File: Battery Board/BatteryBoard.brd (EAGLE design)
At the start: 25.4 x 50.8 mm, 28 parts, among them IC1 TPS63060DSCT, J0 1725656, Q1 IAUC60N04S6L030HATMA1, U0 STM32L031K4U6, U1 MCP73831T-2ATI_OT, U3 STM809TWX6F

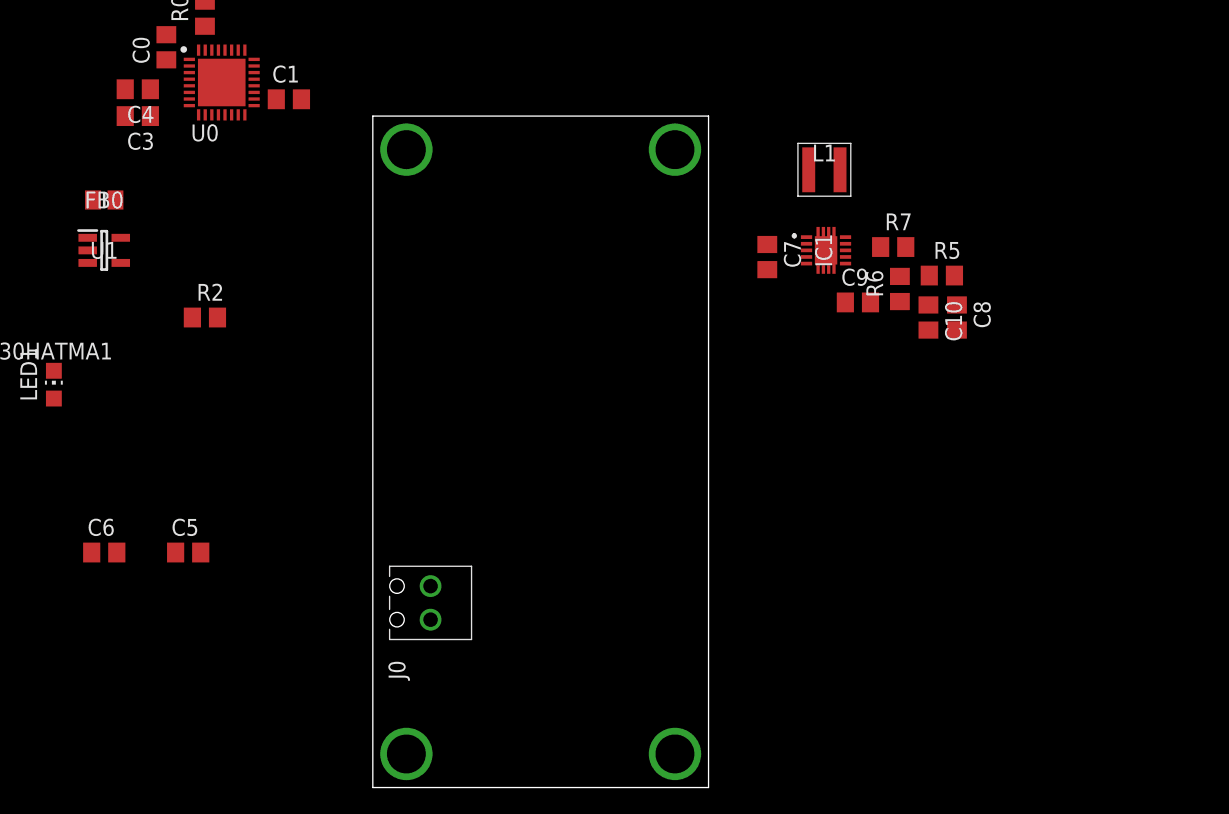
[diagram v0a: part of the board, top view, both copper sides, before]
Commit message: added switch jumper
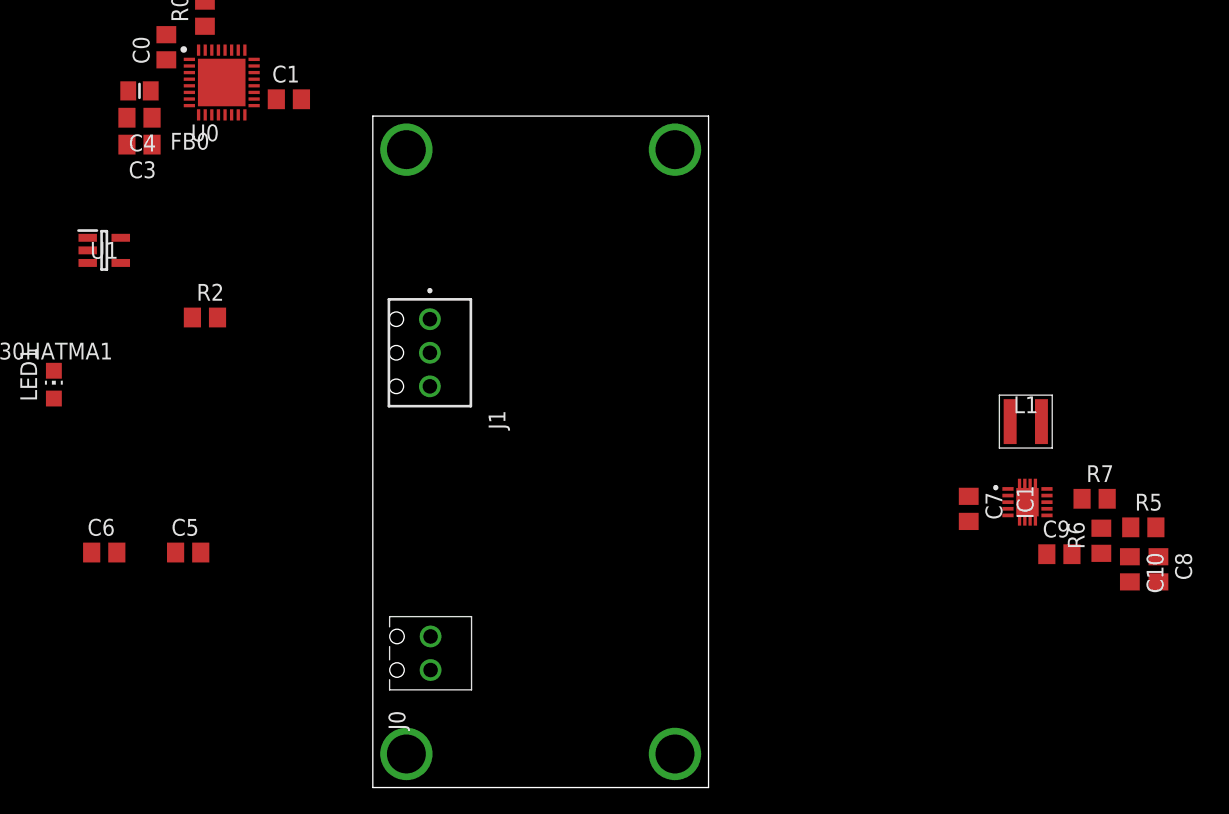
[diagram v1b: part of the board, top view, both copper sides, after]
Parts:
- added J1: 1725669, SamacSys_Parts:1725669
- moved C10 24.4 mm to (44.6, -8.89)
- moved C8 24.4 mm to (46.7, -8.89)
- moved C9 24.4 mm to (39.2, -7.75)
- moved IC1 24.4 mm to (36.8, -3.81)
- moved L1 24.4 mm to (36.7, 2.29)
- moved R5 24.4 mm to (45.6, -5.71)
- moved R6 24.4 mm to (42.4, -6.73)
- moved C7 24.4 mm to (32.4, -4.32)
- moved R7 24.4 mm to (41.9, -3.56)
- moved FB0 8.68 mm to (-30.4, 27.3)
- moved J0 3.81 mm to (-11.4, -15.2)
- moved C3 2.16 mm to (-30.4, 23.2)
- moved C4 2.16 mm to (-30.4, 25.3)
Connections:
- new net SWITCH_IN: J1.2, Q1.4
- net GND: now also J1.3, Q1.5; no longer Q1.2
- net VBAT: now also J1.1

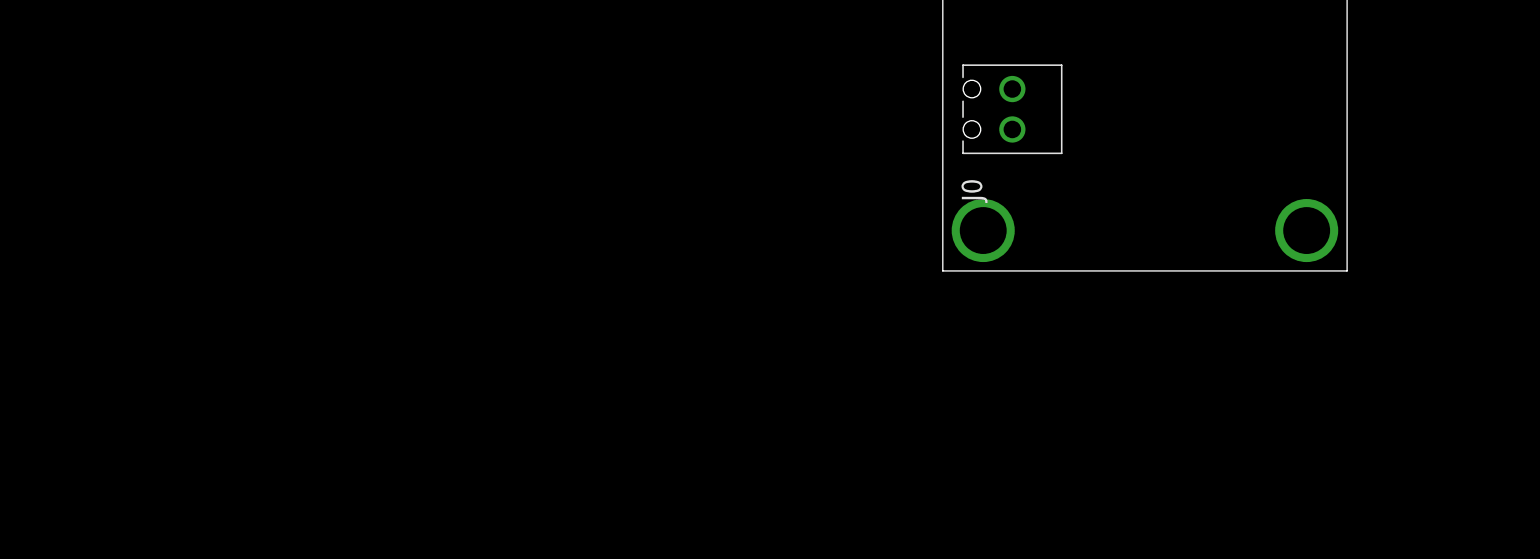
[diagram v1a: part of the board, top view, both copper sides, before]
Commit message: Added USB and 16-pin
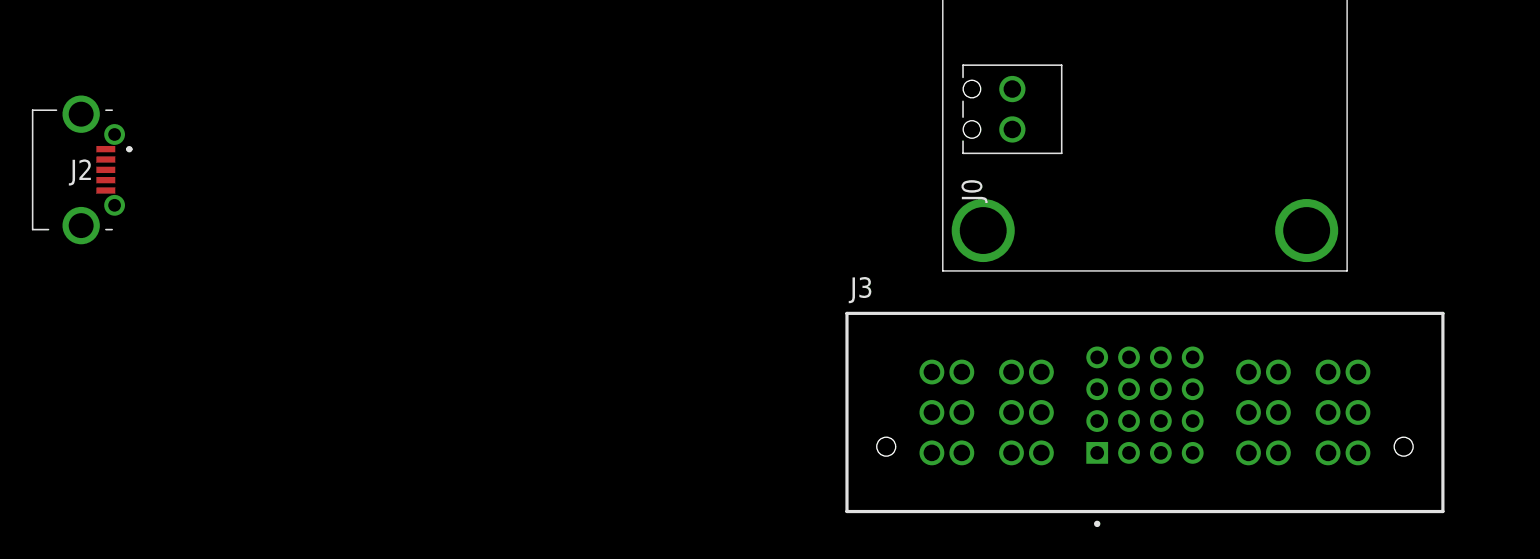
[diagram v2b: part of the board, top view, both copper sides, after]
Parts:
- added J2: UJ2-MIBH2-4-SMT-TR, SamacSys_Parts:UJ2MIBH24SMTTR
- added J3: MPTC-02-16-02-6.30-XX-X-V, MPTC-02-16-02-6.30-XX-X-V:SAMTEC_MPTC-02-16-02-6.30-XX-X-V
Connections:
- new net P02: J3.P02_1, J3.P02_2, J3.P02_3, J3.P02_4, J3.P02_5, J3.P02_6
- new net P03: J3.P03_1, J3.P03_2, J3.P03_3, J3.P03_4, J3.P03_5, J3.P03_6
- net GND: now also J2.5, J2.MH1, J2.MH2, J2.MH3, J2.MH4, J3.P01_1, J3.P01_2, J3.P01_3, J3.P01_4, J3.P01_5, J3.P01_6, J3.P04_1, J3.P04_2, J3.P04_3, J3.P04_4, J3.P04_5, J3.P04_6
- net VUSB: now also J2.1
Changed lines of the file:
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@@
 <attribute name="VALUE" x="-8.382" y="7.493" size="1.27" layer="27" rot="R270" align="center"/>
+</element>
+<element name="J2" library="SamacSys_Parts" package="UJ2MIBH24SMTTR" value="UJ2-MIBH2-4-SMT-TR" x="-67.31" y="-19.05" smashed="yes">
+<attribute name="DESCRIPTION" value="CONN RCPT USB2.0 MICRO B SMD R/A" x="-67.31" y="-19.05" size="1.778" layer="27" display="off"/>
+<attribute name="HEIGHT" value="2.5mm" x="-67.31" y="-19.05" size="1.778" layer="27" display="off"/>
+<attribute name="MANUFACTURER_NAME" value="CUI Inc." x="-67.31" y="-19.05" size="1.778" layer="27" display="off"/>
+<attribute name="MANUFACTURER_PART_NUMBER" value="UJ2-MIBH2-4-SMT-TR" x="-67.31" y="-19.05" size="1.778" layer="27" display="off"/>
+<attribute name="MOUSER_PART_NUMBER" value="490-UJ2-MIBH2-4-SMT" x="-67.31" y="-19.05" size="1.778" layer="27" display="off"/>
+<attribute name="MOUSER_PRICE-STOCK" value="https://www.mouser.co.uk/ProductDetail/CUI-Devices/UJ2-MIBH2-4-SMT-TR/?qs=5mqXD9RfOg1yxHIpPvPxvQ%3D%3D" x="-67.31" y="-19.05" size="1.778" layer="27" display="off"/>
+<attribute name="NAME" x="-66.798" y="-19.05" size="1.27" layer="25" align="center"/>
+<attribute name="VALUE" x="-66.798" y="-19.05" size="1.27" layer="27" align="center"/>
+</element>
+<element name="J3" library="MPTC-02-16-02-6.30-XX-X-V" package="SAMTEC_MPTC-02-16-02-6.30-XX-X-V" value="MPTC-02-16-02-6.30-XX-X-V" x="0" y="-34.29" smashed="yes">
+<attribute name="MANUFACTURER" value="Samtec" x="0" y="-34.29" size="1.778" layer="27" display="off"/>
+<attribute name="MAXIMUM_PACKAGE_HEIGHT" value="11.38 mm" x="0" y="-34.29" size="1.778" layer="27" display="off"/>
+<attribute name="NAME" x="-18.5272" y="-27.07648125" size="1.272390625" layer="25"/>
+<attribute name="PARTREV" value="L" x="0" y="-34.29" size="1.778" layer="27" display="off"/>
+<attribute name="STANDARD" value="Manufacturer Recommendations" x="0" y="-34.29" size="1.778" layer="27" display="off"/>
+<attribute name="VALUE" x="-18.5277" y="-42.7055" size="1.272340625" layer="27"/>
 </element>
 </elements>
@@
 <contactref element="Q1" pad="5"/>
 <contactref element="J1" pad="3"/>
-<wire x1="-51.12" y1="-7.62" x2="-8.382" y2="4.953" width="0" layer="19" extent="1-1"/>
-<wire x1="-59.37" y1="-1.27" x2="-51.12" y2="-7.62" width="0" layer="19" extent="1-1"/>
+<contactref element="J2" pad="5"/>
+<contactref element="J2" pad="MH1"/>
+<contactref element="J2" pad="MH4"/>
+<contactref element="J2" pad="MH2"/>
+<contactref element="J2" pad="MH3"/>
+<contactref element="J3" pad="P01_2"/>
+<contactref element="J3" pad="P01_4"/>
+<contactref element="J3" pad="P01_5"/>
+<contactref element="J3" pad="P01_1"/>
+<contactref element="J3" pad="P01_6"/>
+<contactref element="J3" pad="P01_3"/>
+<contactref element="J3" pad="P04_3"/>
+<contactref element="J3" pad="P04_4"/>
+<contactref element="J3" pad="P04_1"/>
+<contactref element="J3" pad="P04_5"/>
+<contactref element="J3" pad="P04_2"/>
+<contactref element="J3" pad="P04_6"/>
+<wire x1="-11.505" y1="-36.83" x2="-13.385" y2="-36.83" width="0" layer="19" extent="1-1"/>
+<wire x1="-13.385" y1="-34.29" x2="-13.385" y2="-36.83" width="0" layer="19" extent="1-1"/>
+<wire x1="-11.505" y1="-34.29" x2="-13.385" y2="-34.29" width="0" layer="19" extent="1-1"/>
+<wire x1="-13.385" y1="-31.75" x2="-13.385" y2="-34.29" width="0" layer="19" extent="1-1"/>
+<wire x1="-11.505" y1="-31.75" x2="-13.385" y2="-31.75" width="0" layer="19" extent="1-1"/>
+<wire x1="-66.835" y1="-22.55" x2="-11.505" y2="-31.75" width="0" layer="19" extent="1-1"/>
+<wire x1="-64.735" y1="-21.275" x2="-66.835" y2="-22.55" width="0" layer="19" extent="1-1"/>
+<wire x1="-65.285" y1="-20.35" x2="-64.735" y2="-21.275" width="0" layer="19" extent="1-1"/>
+<wire x1="-64.735" y1="-16.825" x2="-65.285" y2="-20.35" width="0" layer="19" extent="1-1"/>
+<wire x1="-66.835" y1="-15.55" x2="-64.735" y2="-16.825" width="0" layer="19" extent="1-1"/>
+<wire x1="-59.37" y1="-1.27" x2="-66.835" y2="-15.55" width="0" layer="19" extent="1-1"/>
+<wire x1="-51.12" y1="-7.62" x2="-59.37" y2="-1.27" width="0" layer="19" extent="1-1"/>
 <wire x1="-48.984996875" y1="5.715" x2="-59.37" y2="-1.27" width="0" layer="19" extent="1-1"/>
 <wire x1="-50.58" y1="16.27" x2="-48.984996875" y2="5.715" width="0" layer="19" extent="1-1"/>
 <wire x1="-34.27" y1="15.24" x2="-50.58" y2="16.27" width="0" layer="19" extent="1-1"/>
-<wire x1="-26.35" y1="10.16" x2="-34.27" y2="15.24" width="0" layer="19" extent="1-1"/>
 <wire x1="-31.303" y1="23.241" x2="-34.27" y2="15.24" width="0" layer="19" extent="1-1"/>
 <wire x1="-31.303" y1="25.273" x2="-31.303" y2="23.241" width="0" layer="19" extent="1-1"/>
 <wire x1="-28.321" y1="31.557" x2="-31.303" y2="25.273" width="0" layer="19" extent="1-1"/>
+<wire x1="-26.35" y1="10.16" x2="-34.27" y2="15.24" width="0" layer="19" extent="1-1"/>
 <wire x1="-18.1" y1="26.67" x2="-28.321" y2="31.557" width="0" layer="19" extent="1-1"/>
 <wire x1="-25.72" y1="-7.62" x2="-26.35" y2="10.16" width="0" layer="19" extent="1-1"/>
 <wire x1="-32.07" y1="-7.62" x2="-25.72" y2="-7.62" width="0" layer="19" extent="1-1"/>
+<wire x1="-8.382" y1="4.953" x2="-26.35" y2="10.16" width="0" layer="19" extent="1-1"/>
 <wire x1="-8.33" y1="-16.51" x2="-25.72" y2="-7.62" width="0" layer="19" extent="1-1"/>
-<wire x1="32.385" y1="-5.268" x2="-8.33" y2="-16.51" width="0" layer="19" extent="1-1"/>
+<wire x1="11.505" y1="-36.83" x2="-11.505" y2="-36.83" width="0" layer="19" extent="1-1"/>
+<wire x1="13.385" y1="-36.83" x2="11.505" y2="-36.83" width="0" layer="19" extent="1-1"/>
+<wire x1="11.505" y1="-34.29" x2="11.505" y2="-36.83" width="0" layer="19" extent="1-1"/>
+<wire x1="13.385" y1="-34.29" x2="11.505" y2="-34.29" width="0" layer="19" extent="1-1"/>
+<wire x1="11.505" y1="-31.75" x2="11.505" y2="-34.29" width="0" layer="19" extent="1-1"/>
+<wire x1="13.385" y1="-31.75" x2="11.505" y2="-31.75" width="0" layer="19" extent="1-1"/>
+<wire x1="32.385" y1="-5.268" x2="-8.382" y2="4.953" width="0" layer="19" extent="1-1"/>
 <wire x1="35.355" y1="-4.31" x2="32.385" y2="-5.268" width="0" layer="19" extent="1-1"/>
 <wire x1="36.83" y1="-3.81" x2="35.355" y2="-4.31" width="0" layer="19" extent="1-1"/>
@@
 <contactref element="C5" pad="1"/>
 <contactref element="LED1" pad="A"/>
-<wire x1="-36.83" y1="4.03" x2="-31.77" y2="14.29" width="0" layer="19" extent="1-1"/>
+<contactref element="J2" pad="1"/>
+<wire x1="-36.83" y1="4.03" x2="-65.285" y2="-17.75" width="0" layer="19" extent="1-1"/>
+<wire x1="-31.77" y1="14.29" x2="-36.83" y2="4.03" width="0" layer="19" extent="1-1"/>
 <wire x1="-27.62" y1="-7.62" x2="-36.83" y2="4.03" width="0" layer="19" extent="1-1"/>
 </signal>
@@
 <wire x1="-55.040003125" y1="5.715" x2="-8.382" y2="7.493" width="0" layer="19" extent="1-1"/>
 </signal>
+<signal name="P03">
+<contactref element="J3" pad="P03_3"/>
+<contactref element="J3" pad="P03_1"/>
+<contactref element="J3" pad="P03_4"/>
+<contactref element="J3" pad="P03_6"/>
+<contactref element="J3" pad="P03_5"/>
+<contactref element="J3" pad="P03_2"/>
+<wire x1="8.385" y1="-36.83" x2="6.505" y2="-36.83" width="0" layer="19" extent="1-1"/>
+<wire x1="6.505" y1="-34.29" x2="6.505" y2="-36.83" width="0" layer="19" extent="1-1"/>
+<wire x1="8.385" y1="-34.29" x2="6.505" y2="-34.29" width="0" layer="19" extent="1-1"/>
+<wire x1="6.505" y1="-31.75" x2="6.505" y2="-34.29" width="0" layer="19" extent="1-1"/>
+<wire x1="8.385" y1="-31.75" x2="6.505" y2="-31.75" width="0" layer="19" extent="1-1"/>
+</signal>
+<signal name="P02">
+<contactref element="J3" pad="P02_1"/>
+<contactref element="J3" pad="P02_2"/>
+<contactref element="J3" pad="P02_3"/>
+<contactref element="J3" pad="P02_4"/>
+<contactref element="J3" pad="P02_5"/>
+<contactref element="J3" pad="P02_6"/>
+<wire x1="-6.505" y1="-36.83" x2="-8.385" y2="-36.83" width="0" layer="19" extent="1-1"/>
+<wire x1="-8.385" y1="-34.29" x2="-8.385" y2="-36.83" width="0" layer="19" extent="1-1"/>
+<wire x1="-6.505" y1="-34.29" x2="-8.385" y2="-34.29" width="0" layer="19" extent="1-1"/>
+<wire x1="-8.385" y1="-31.75" x2="-8.385" y2="-34.29" width="0" layer="19" extent="1-1"/>
+<wire x1="-6.505" y1="-31.75" x2="-8.385" y2="-31.75" width="0" layer="19" extent="1-1"/>
+</signal>
 </signals>

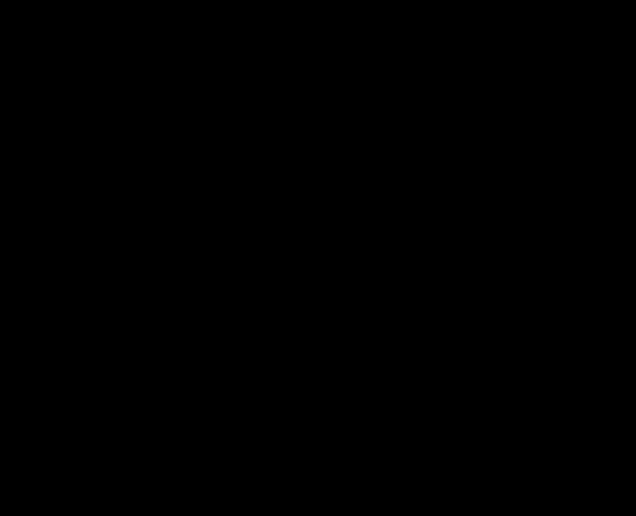
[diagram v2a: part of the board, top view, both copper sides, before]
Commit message: Added JSTPH2
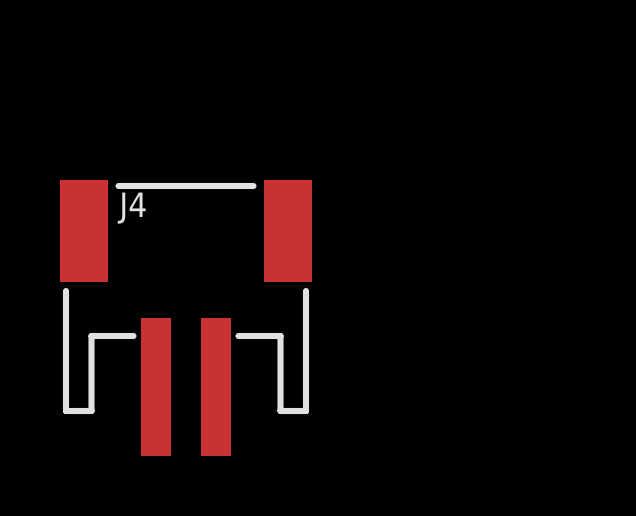
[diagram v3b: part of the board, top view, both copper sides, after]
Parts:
- added J4: JSTPH2, Connect:JSTPH2
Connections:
- net GND: now also J4.1
- net VBAT: now also J4.2
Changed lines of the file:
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@@
 <attribute name="VALUE" x="-18.5277" y="-42.7055" size="1.272340625" layer="27"/>
+</element>
+<element name="J4" library="Connect" package="JSTPH2" package3d_urn="urn:adsk.eagle:package:15955189/2" value="JSTPH2" x="-90.17" y="-36.83" smashed="yes">
+<attribute name="NAME" x="-92.3925" y="-34.8615" size="0.8128" layer="25" ratio="18"/>
+<attribute name="VALUE" x="-92.3925" y="-35.56" size="0.4064" layer="27" ratio="10"/>
 </element>
 </elements>
@@
 <contactref element="J3" pad="P04_2"/>
 <contactref element="J3" pad="P04_6"/>
-<wire x1="-11.505" y1="-36.83" x2="-13.385" y2="-36.83" width="0" layer="19" extent="1-1"/>
-<wire x1="-13.385" y1="-34.29" x2="-13.385" y2="-36.83" width="0" layer="19" extent="1-1"/>
-<wire x1="-11.505" y1="-34.29" x2="-13.385" y2="-34.29" width="0" layer="19" extent="1-1"/>
-<wire x1="-13.385" y1="-31.75" x2="-13.385" y2="-34.29" width="0" layer="19" extent="1-1"/>
-<wire x1="-11.505" y1="-31.75" x2="-13.385" y2="-31.75" width="0" layer="19" extent="1-1"/>
-<wire x1="-66.835" y1="-22.55" x2="-11.505" y2="-31.75" width="0" layer="19" extent="1-1"/>
+<contactref element="J4" pad="1"/>
+<wire x1="-66.835" y1="-22.55" x2="-91.17" y2="-40.53" width="0" layer="19" extent="1-1"/>
 <wire x1="-64.735" y1="-21.275" x2="-66.835" y2="-22.55" width="0" layer="19" extent="1-1"/>
 <wire x1="-65.285" y1="-20.35" x2="-64.735" y2="-21.275" width="0" layer="19" extent="1-1"/>
@@
 <wire x1="-8.382" y1="4.953" x2="-26.35" y2="10.16" width="0" layer="19" extent="1-1"/>
 <wire x1="-8.33" y1="-16.51" x2="-25.72" y2="-7.62" width="0" layer="19" extent="1-1"/>
+<wire x1="-11.505" y1="-31.75" x2="-8.33" y2="-16.51" width="0" layer="19" extent="1-1"/>
+<wire x1="-13.385" y1="-31.75" x2="-11.505" y2="-31.75" width="0" layer="19" extent="1-1"/>
+<wire x1="-13.385" y1="-34.29" x2="-13.385" y2="-31.75" width="0" layer="19" extent="1-1"/>
+<wire x1="-11.505" y1="-34.29" x2="-13.385" y2="-34.29" width="0" layer="19" extent="1-1"/>
+<wire x1="-13.385" y1="-36.83" x2="-13.385" y2="-34.29" width="0" layer="19" extent="1-1"/>
+<wire x1="-11.505" y1="-36.83" x2="-13.385" y2="-36.83" width="0" layer="19" extent="1-1"/>
 <wire x1="11.505" y1="-36.83" x2="-11.505" y2="-36.83" width="0" layer="19" extent="1-1"/>
 <wire x1="13.385" y1="-36.83" x2="11.505" y2="-36.83" width="0" layer="19" extent="1-1"/>
@@
 <wire x1="11.505" y1="-31.75" x2="11.505" y2="-34.29" width="0" layer="19" extent="1-1"/>
 <wire x1="13.385" y1="-31.75" x2="11.505" y2="-31.75" width="0" layer="19" extent="1-1"/>
-<wire x1="32.385" y1="-5.268" x2="-8.382" y2="4.953" width="0" layer="19" extent="1-1"/>
+<wire x1="32.385" y1="-5.268" x2="13.385" y2="-31.75" width="0" layer="19" extent="1-1"/>
 <wire x1="35.355" y1="-4.31" x2="32.385" y2="-5.268" width="0" layer="19" extent="1-1"/>
 <wire x1="36.83" y1="-3.81" x2="35.355" y2="-4.31" width="0" layer="19" extent="1-1"/>
@@
 <contactref element="C7" pad="1"/>
 <contactref element="J1" pad="1"/>
-<wire x1="-33.97" y1="-7.62" x2="-8.382" y2="10.033" width="0" layer="19" extent="1-1"/>
-<wire x1="-34.27" y1="14.29" x2="-33.97" y2="-7.62" width="0" layer="19" extent="1-1"/>
-<wire x1="-48.48" y1="15.24" x2="-34.27" y2="14.29" width="0" layer="19" extent="1-1"/>
-<wire x1="-58.74" y1="3.81" x2="-48.48" y2="15.24" width="0" layer="19" extent="1-1"/>
-<wire x1="-8.33" y1="-13.97" x2="-33.97" y2="-7.62" width="0" layer="19" extent="1-1"/>
+<contactref element="J4" pad="2"/>
+<wire x1="-58.74" y1="3.81" x2="-89.17" y2="-40.53" width="0" layer="19" extent="1-1"/>
+<wire x1="-48.48" y1="15.24" x2="-58.74" y2="3.81" width="0" layer="19" extent="1-1"/>
+<wire x1="-34.27" y1="14.29" x2="-48.48" y2="15.24" width="0" layer="19" extent="1-1"/>
+<wire x1="-33.97" y1="-7.62" x2="-34.27" y2="14.29" width="0" layer="19" extent="1-1"/>
+<wire x1="-8.382" y1="10.033" x2="-34.27" y2="14.29" width="0" layer="19" extent="1-1"/>
+<wire x1="-8.33" y1="-13.97" x2="-8.382" y2="10.033" width="0" layer="19" extent="1-1"/>
 <wire x1="32.385" y1="-3.368" x2="-8.33" y2="-13.97" width="0" layer="19" extent="1-1"/>
 <wire x1="35.355" y1="-3.31" x2="32.385" y2="-3.368" width="0" layer="19" extent="1-1"/>
